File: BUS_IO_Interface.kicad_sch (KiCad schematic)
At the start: 39 parts, among them U12 MAX31331TETB+, U13 AS1016204-0108X0PWAY, U14 TCAN1044ADDFRQ1, U16 AS1016204-0108X0PWAY, U18 AS1016204-0108X0PWAY, U20 AS1016204-0108X0PWAY, U22 TCAN1044ADDFRQ1, Y3 32.768kHz

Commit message: Rework passives around the CPU to be 0402
Signed-off-by: Corey Minyard <corey@minyard.net>
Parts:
- R46: footprint Resistor_SMD:R_0603_1608Metric_Pad0.98x0.95mm_HandSolder -> Resistor_SMD:R_0402_1005Metric_Pad0.72x0.64mm_HandSolder
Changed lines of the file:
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@@
 			)
 		)
-		(property "Footprint" "Resistor_SMD:R_0603_1608Metric_Pad0.98x0.95mm_HandSolder"
+		(property "Footprint" "Resistor_SMD:R_0402_1005Metric_Pad0.72x0.64mm_HandSolder"
 			(at 78.74 69.088 90)
 			(effects

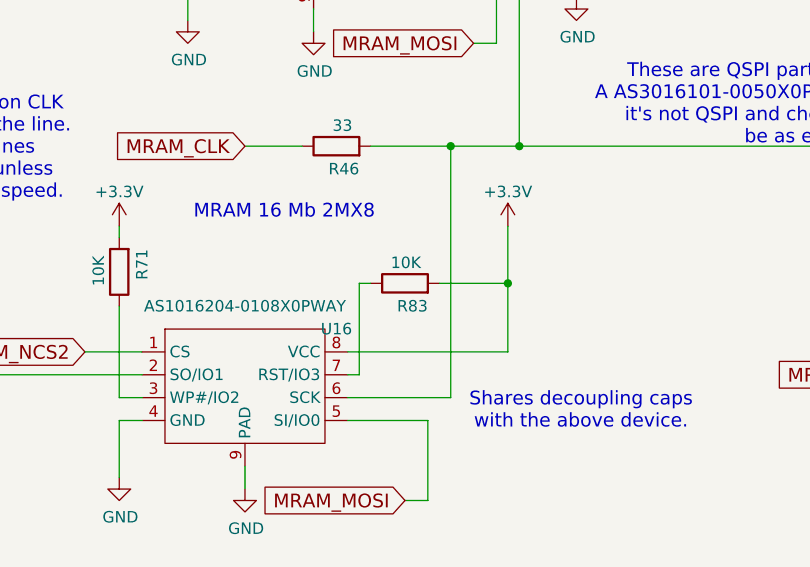
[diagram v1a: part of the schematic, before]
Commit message: Change clock and MRAM passives to 0402
Signed-off-by: Corey Minyard <corey@minyard.net>
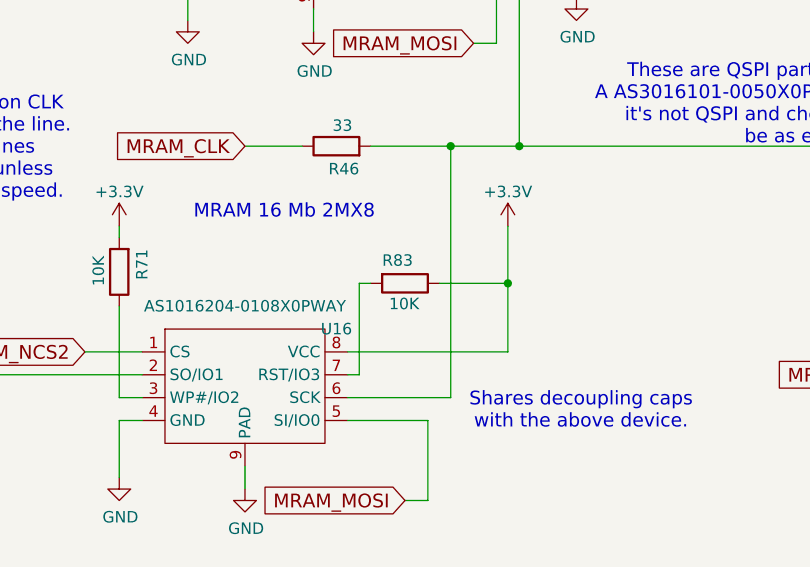
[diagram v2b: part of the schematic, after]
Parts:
- C43, C45, C98, C99: footprint Capacitor_SMD:C_0603_1608Metric_Pad1.08x0.95mm_HandSolder -> Capacitor_SMD:C_0402_1005Metric_Pad0.74x0.62mm_HandSolder
- R61, R66, R71, R83, R84, R85, R86, R87: footprint Resistor_SMD:R_0603_1608Metric_Pad0.98x0.95mm_HandSolder -> Resistor_SMD:R_0402_1005Metric_Pad0.72x0.64mm_HandSolder
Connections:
- net +3.3V: now also R83.1; no longer R83.2
- net at U16.7 (RST/IO3): now also R83.2; no longer R83.1

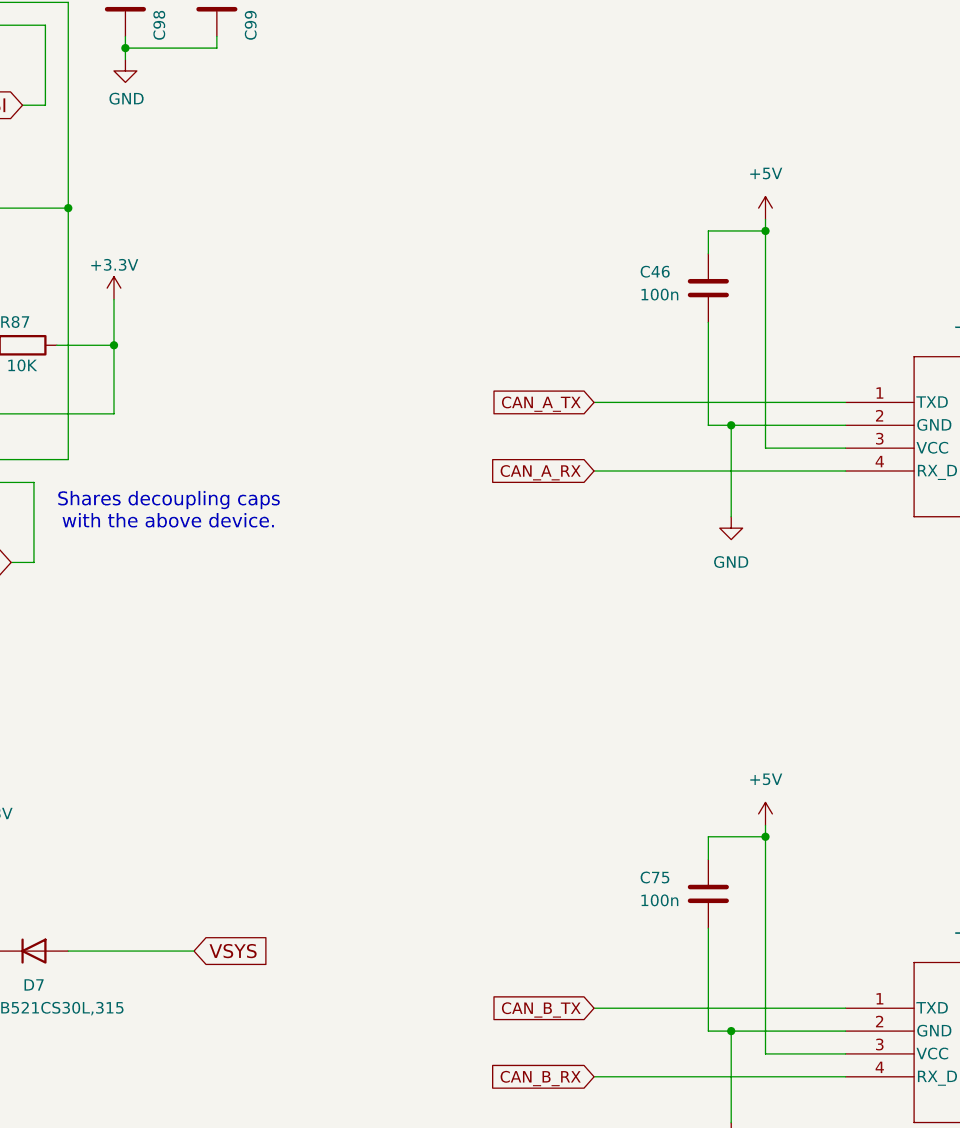
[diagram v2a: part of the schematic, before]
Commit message: Add a current limiter for on-board +5V devices
Signed-off-by: Corey Minyard <corey@minyard.net>
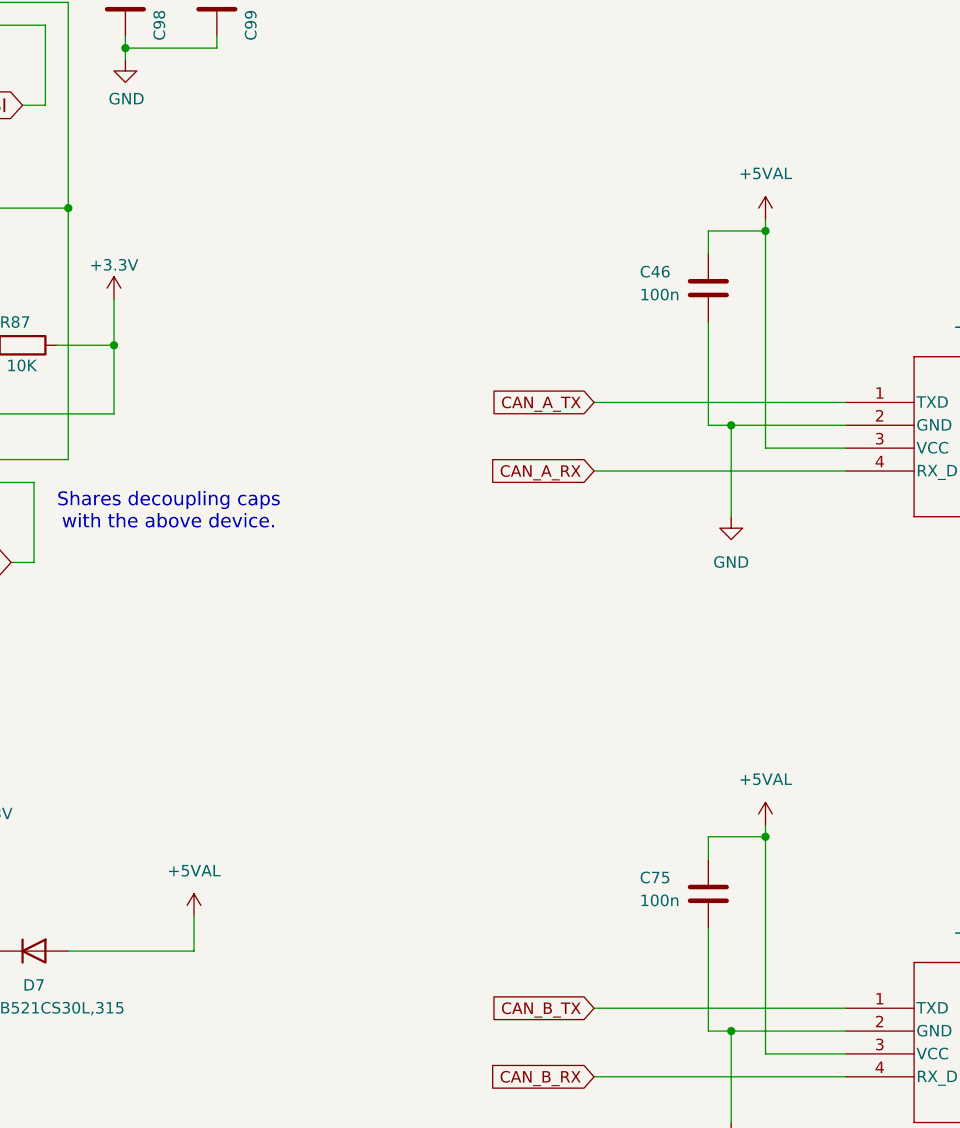
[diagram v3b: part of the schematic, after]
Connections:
- net VSYS is gone; now on net +5VAL: D7.2 (A)
- net +5V renamed +5VAL
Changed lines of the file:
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@@
 	(wire
 		(pts
+			(xy 218.44 146.05) (xy 218.44 149.86)
+		)
+		(stroke
+			(width 0)
+			(type default)
+		)
+	)
+	(wire
+		(pts
 			(xy 146.05 133.35) (xy 146.05 149.86)
 		)
@@
 		)
 	)
-	(global_label "VSYS"
-		(shape input)
-		(at 218.44 149.86 0)
-		(fields_autoplaced yes)
-		(effects
-			(font
-				(size 1.524 1.524)
-			)
-			(justify left)
-		)
-		(property "Intersheetrefs" "${INTERSHEET_REFS}"
-			(at 226.6568 149.86 0)
-			(effects
-				(font
-					(size 1.27 1.27)
-				)
-				(justify left)
-				(hide yes)
-			)
-		)
-	)
 	(global_label "CAN_B_TX"
 		(shape input)
@@
 			)
 		)
-		(property "Value" "+5V"
+		(property "Value" "+5VAL"
 			(at 281.94 63.5 0)
 			(effects
@@
 	)
 	(symbol
+		(lib_id "power:+5V")
+		(at 218.44 146.05 0)
+		(unit 1)
+		(exclude_from_sim no)
+		(in_bom yes)
+		(on_board yes)
+		(dnp no)
+		(fields_autoplaced yes)
+		(property "Reference" "#PWR0290"
+			(at 218.44 149.86 0)
+			(effects
+				(font
+					(size 1.27 1.27)
+				)
+				(hide yes)
+			)
+		)
+		(property "Value" "+5VAL"
+			(at 218.44 140.97 0)
+			(effects
+				(font
+					(size 1.27 1.27)
+				)
+			)
+		)
+		(property "Footprint" ""
+			(at 218.44 146.05 0)
+			(effects
+				(font
+					(size 1.27 1.27)
+				)
+				(hide yes)
+			)
+		)
+		(property "Datasheet" ""
+			(at 218.44 146.05 0)
+			(effects
+				(font
+					(size 1.27 1.27)
+				)
+				(hide yes)
+			)
+		)
+		(property "Description" "Power symbol creates a global label with name \"+5V\""
+			(at 218.44 146.05 0)
+			(effects
+				(font
+					(size 1.27 1.27)
+				)
+				(hide yes)
+			)
+		)
+		(pin "1"
+		)
+		(instances
+			(project "PacSat_AFSK"
+				(path "/cc9f42d2-6985-41ac-acab-5ab7b01c5b38/aff81ec5-748c-4fc9-b1e8-df12a16f6289"
+					(reference "#PWR0290")
+					(unit 1)
+				)
+			)
+		)
+	)
+	(symbol
 		(lib_id "PACSAT_ICs:QSPI_FLASH_WSON_8-pin")
 		(at 76.2 43.18 0)
@@
 			)
 		)
-		(property "Value" "+5V"
+		(property "Value" "+5VAL"
 			(at 281.94 130.81 0)
 			(effects

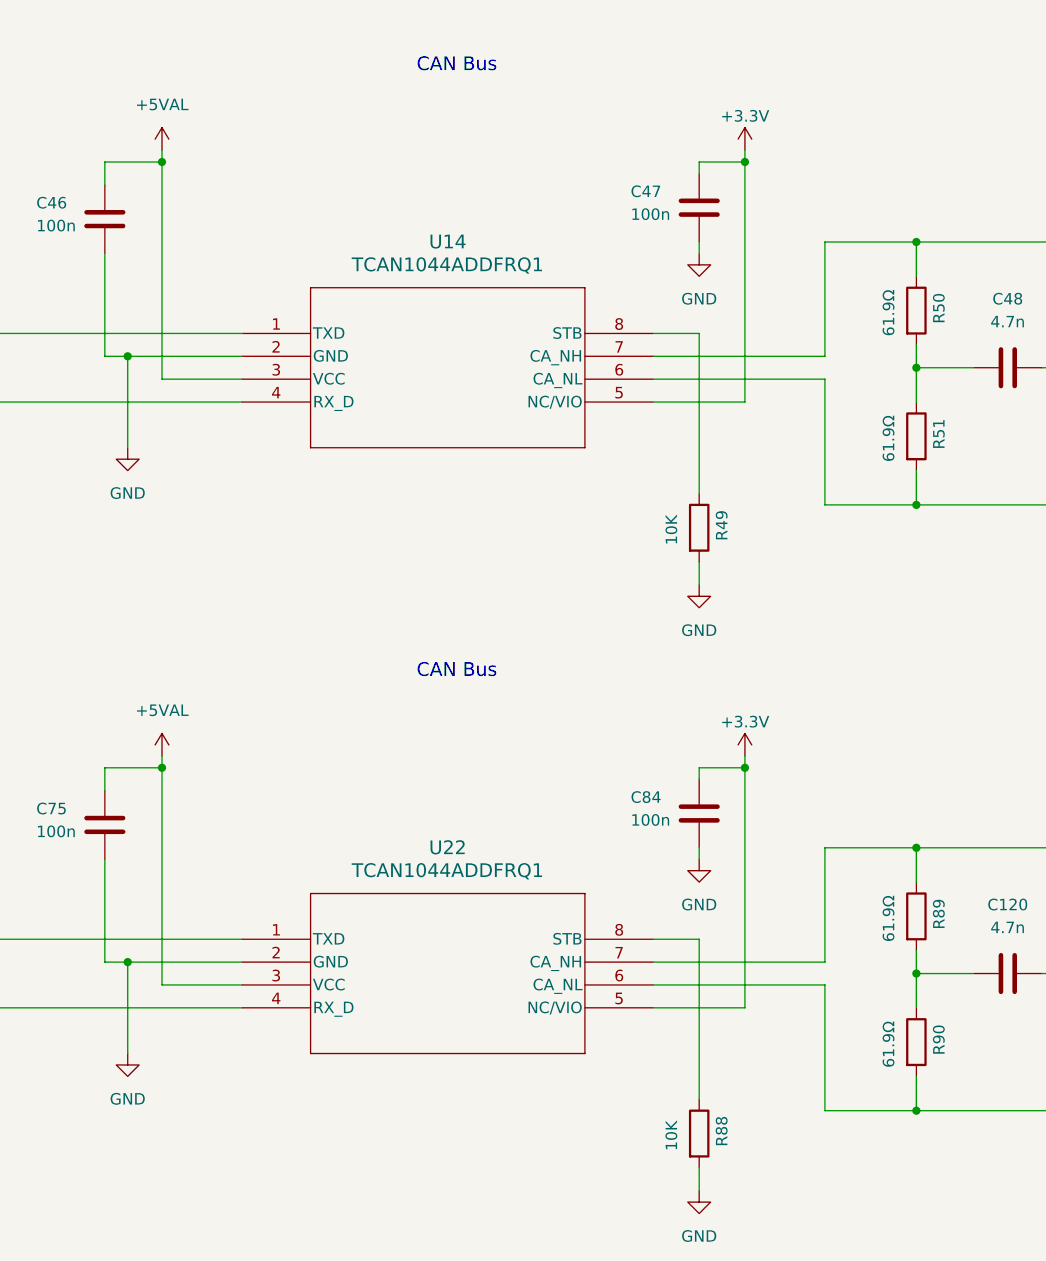
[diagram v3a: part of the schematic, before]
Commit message: Add enable controls for the CAN bus transceivers
And do some more 0402 conversions.

Signed-off-by: Corey Minyard <corey@minyard.net>
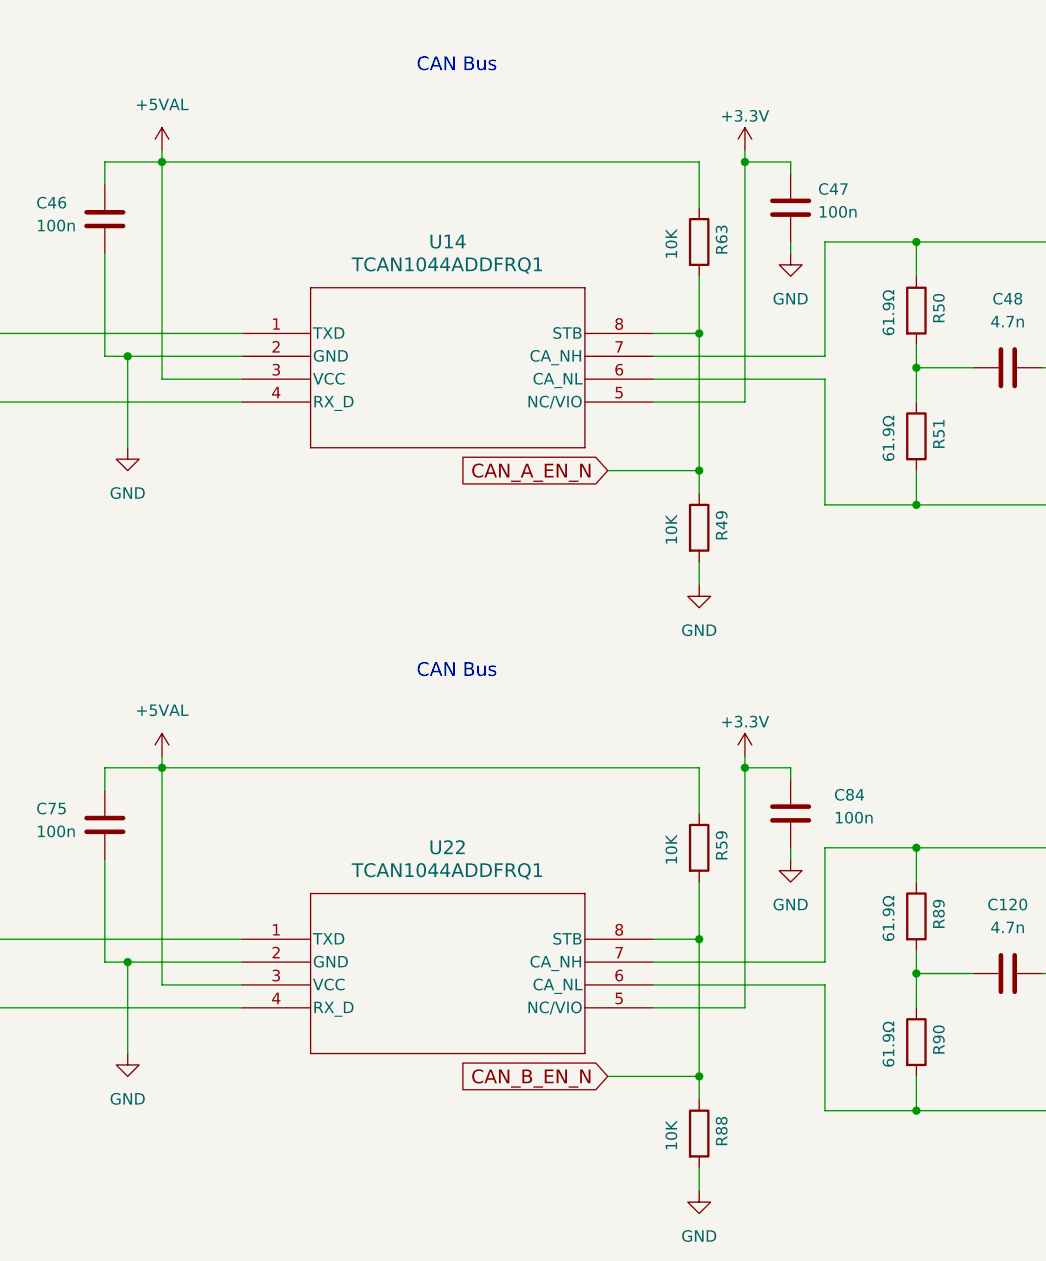
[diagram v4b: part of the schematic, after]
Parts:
- added R59, R63: 10K, Resistor_SMD:R_0402_1005Metric_Pad0.72x0.64mm_HandSolder, symbol Device:R
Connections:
- net +5VAL: now also R59.1, R63.1
- net CAN_B_EN_N: now reaches R88.1, U22.8 (STB)
- net CAN_B_EN_N: now also R59.2
- net CAN_A_EN_N: now reaches R49.1, U14.8 (STB)
- net CAN_A_EN_N: now also R63.2
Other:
- moved on the sheet: C47, C84

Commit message: Work on cleaning up all values for things
Signed-off-by: Corey Minyard <corey@minyard.net>
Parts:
- C44: value .1u -> 100n
- R44, R45: value 4k7 -> 4.7K
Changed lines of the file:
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@@
 		)
 		(property "Value" "47u 10V"
-			(at 160.02 153.67 90)
+			(at 159.766 156.464 90)
 			(effects
 				(font
@@
 			)
 		)
-		(property "Value" "4k7"
+		(property "Value" "4.7K"
 			(at 88.392 175.387 0)
 			(effects
@@
 			)
 		)
-		(property "Value" ".1u"
-			(at 175.26 156.21 90)
+		(property "Value" "100n"
+			(at 175.26 158.242 90)
 			(effects
 				(font
@@
 			)
 		)
-		(property "Value" "4k7"
-			(at 97.79 175.26 0)
+		(property "Value" "4.7K"
+			(at 99.314 175.26 0)
 			(effects
 				(font
